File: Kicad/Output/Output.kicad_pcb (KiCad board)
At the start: 2 copper layers, 93.7 x 58.7 mm, 13 parts, among them J1 Conn_01x02, J2 Conn_01x03

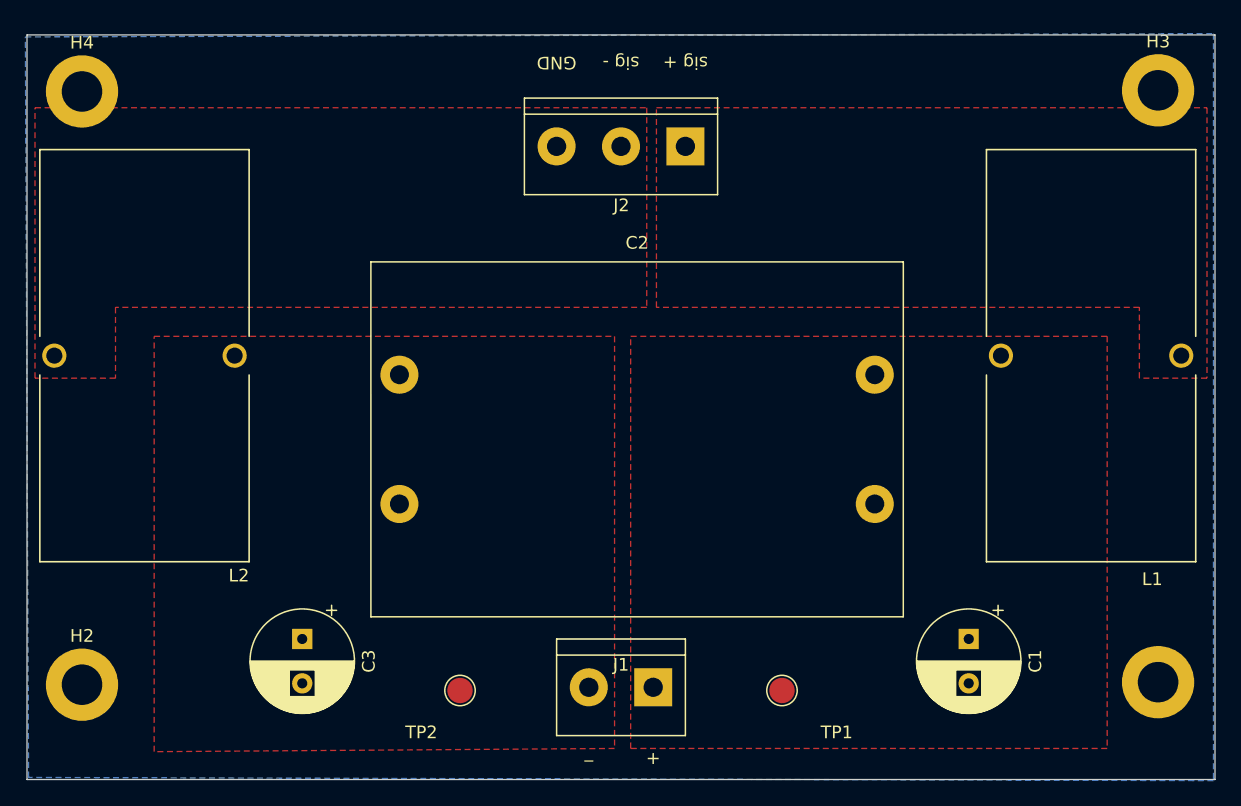
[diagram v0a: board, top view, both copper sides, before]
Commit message: Make Output Filter Board Smaller
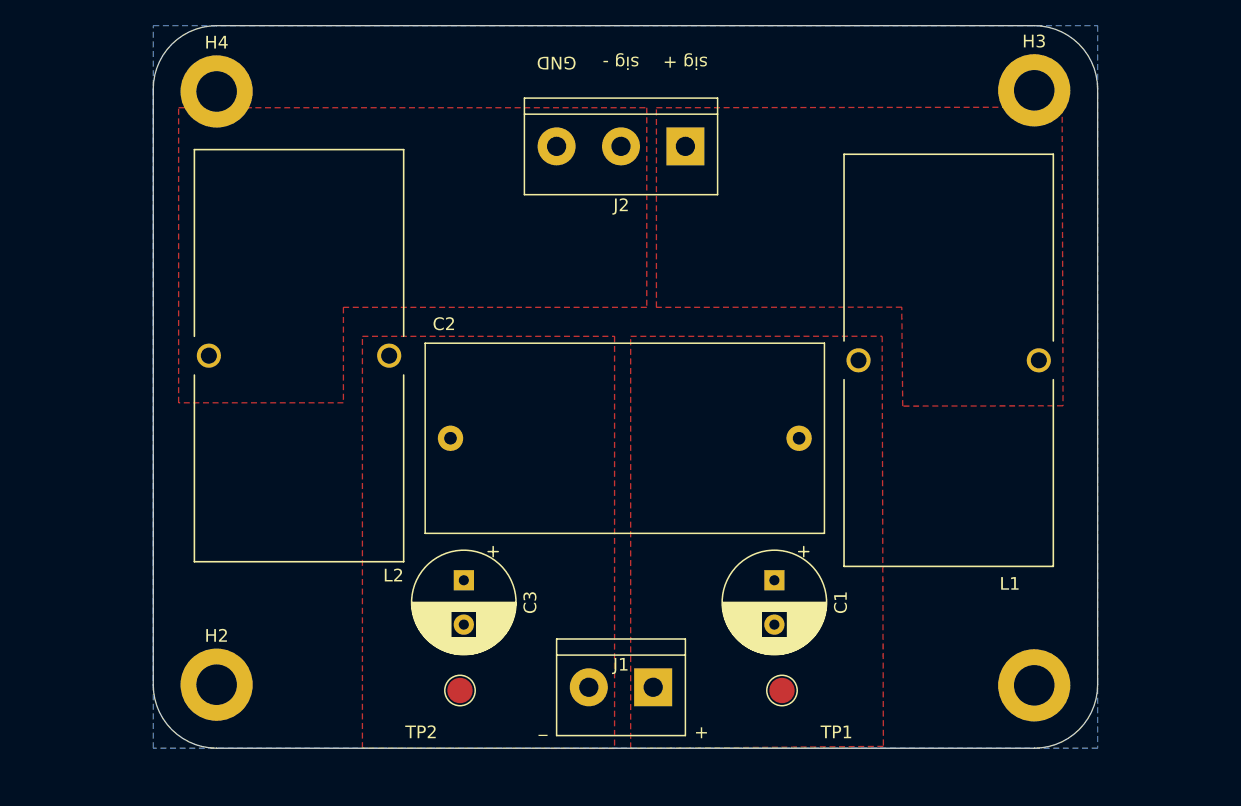
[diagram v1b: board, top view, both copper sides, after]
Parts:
- C2: footprint OutputFilmCapacitor:C4AQQBW5140A3JJ -> OutputFilmCapacitor:C4AQLBU5140M18K
- moved C1 16.0 mm to (164.5, 115.0)
- moved C3 13.6 mm to (140.0, 115.0)
- moved C2 12.9 mm to (145.4, 97.8)
- moved L2 12.2 mm to (127.0, 97.3)
- moved L1 11.2 mm to (178.2, 97.7)
- moved H2 10.6 mm to (120.5, 123.2)
- moved H4 10.6 mm to (120.5, 76.4)
- moved H1 9.77 mm to (185.0, 123.3)
- moved H3 9.77 mm to (185.0, 76.3)
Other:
- board size 93.7 x 58.7 mm -> 74.5 x 57 mm
